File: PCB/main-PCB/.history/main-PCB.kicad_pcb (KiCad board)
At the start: 4 copper layers, 19.9 x 18.2 mm, 25 parts, among them Q1 SSM6J214FE, Q2 Q_NMOS_GSD, U1 LIS2DU12TR, U2 STM32U031K4Ux

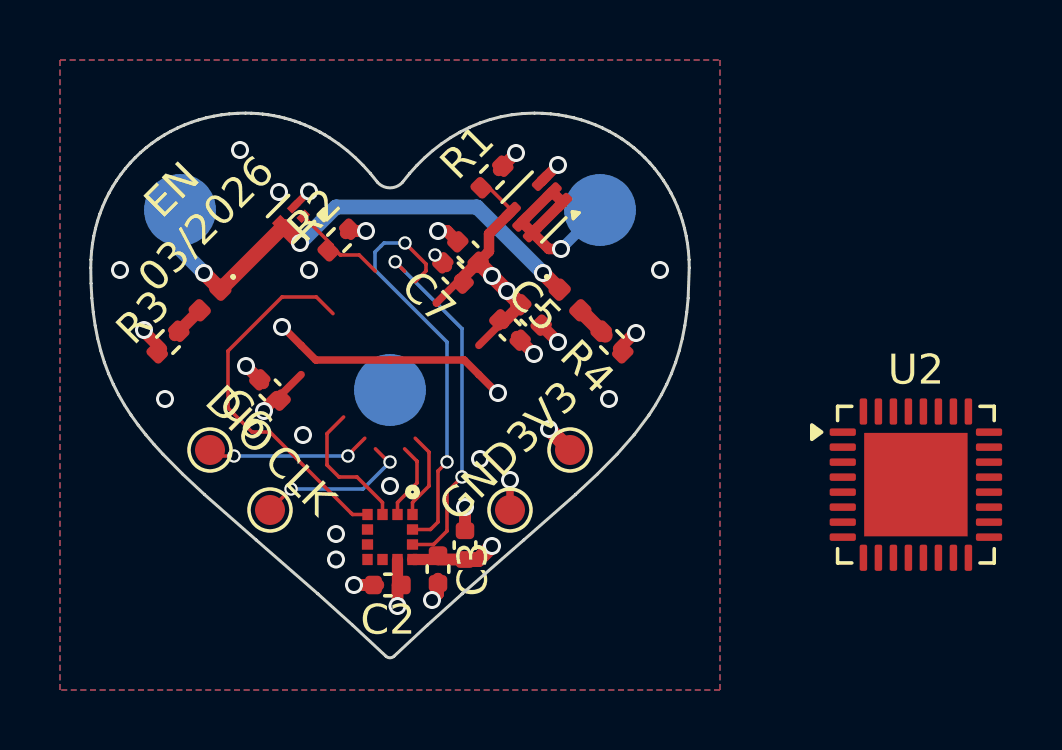
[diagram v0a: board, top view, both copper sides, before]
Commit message: -Updated MCU part number -Changed to 0402 passives
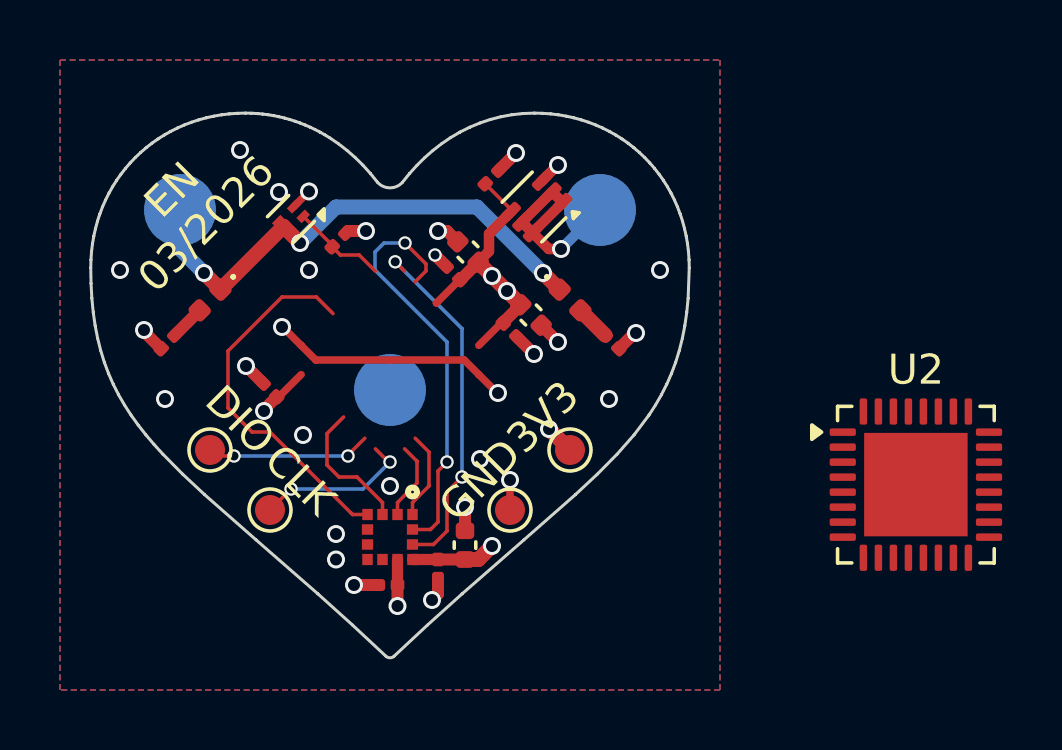
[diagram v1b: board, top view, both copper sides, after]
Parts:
- C2, C3, C5, C6, C7: footprint Capacitor_SMD:C_0402_1005Metric -> Capacitor_SMD:C_0201_0603Metric
- R1, R2, R3, R4: footprint Resistor_SMD:R_0402_1005Metric -> Resistor_SMD:R_0201_0603Metric

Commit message: Updated PCB STEP file
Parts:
- removed the TP5 at (156.0, 93.0)
- added C5: 100nF, Capacitor_SMD:C_0402_1005Metric, F.Cu at (154.7, 91.4)
- added REF**: Val**, EN_Designs-Footprints:JLCPCB_Mouse_Bite, F.Cu at (145.5, 96.3)
- added REF**: Val**, EN_Designs-Footprints:JLCPCB_Mouse_Bite, F.Cu at (156.3, 94.7)
- added REF**: Val**, EN_Designs-Footprints:JLCPCB_Mouse_Bite, F.Cu at (151.1, 99.3)
- added REF**: Val**, EN_Designs-Footprints:JLCPCB_Mouse_Bite, F.Cu at (143.7, 94.7)
- added REF**: Val**, EN_Designs-Footprints:JLCPCB_Mouse_Bite, F.Cu at (151.9, 98.6)
- added REF**: Val**, EN_Designs-Footprints:JLCPCB_Mouse_Bite, F.Cu at (146.4, 97.1)
- added REF**: Val**, EN_Designs-Footprints:JLCPCB_Mouse_Bite, F.Cu at (155.4, 95.5)
- added REF**: Val**, EN_Designs-Footprints:JLCPCB_Mouse_Bite, F.Cu at (142.8, 93.9)
- added REF**: Val**, EN_Designs-Footprints:JLCPCB_Mouse_Bite, F.Cu at (148.9, 99.3)
- added REF**: Val**, EN_Designs-Footprints:JLCPCB_Mouse_Bite, F.Cu at (144.6, 95.5)
- added REF**: Val**, EN_Designs-Footprints:JLCPCB_Mouse_Bite, F.Cu at (147.2, 97.8)
- added REF**: Val**, EN_Designs-Footprints:JLCPCB_Mouse_Bite, F.Cu at (154.5, 96.3)
- added REF**: Val**, EN_Designs-Footprints:JLCPCB_Mouse_Bite, F.Cu at (148.1, 98.6)
- added REF**: Val**, EN_Designs-Footprints:JLCPCB_Mouse_Bite, F.Cu at (153.6, 97.1)
- added REF**: Val**, EN_Designs-Footprints:JLCPCB_Mouse_Bite, F.Cu at (152.8, 97.8)
- added REF**: Val**, EN_Designs-Footprints:JLCPCB_Mouse_Bite, F.Cu at (157.2, 93.9)
- added TP2: TestPoint, TestPoint:TestPoint_Pad_D1.0mm, F.Cu at (157.0, 92.0)
- added TP4: TestPoint, EN_Designs-Footprints:TestPoint_Pad_D0.5mm, F.Cu at (155.7, 90.4)
- C2, C3: footprint Capacitor_SMD:C_0201_0603Metric -> Capacitor_SMD:C_0402_1005Metric
- C6: renamed from C5; footprint Capacitor_SMD:C_0201_0603Metric -> Capacitor_SMD:C_0402_1005Metric
- C7: renamed from C6; footprint Capacitor_SMD:C_0201_0603Metric -> Capacitor_SMD:C_0402_1005Metric
- C8: renamed from C7; footprint Capacitor_SMD:C_0201_0603Metric -> Capacitor_SMD:C_0402_1005Metric
- R1, R2, R3, R4: footprint Resistor_SMD:R_0201_0603Metric -> Resistor_SMD:R_0402_1005Metric
- moved U2 18.0 mm to (150.0, 90.0), turned to -135 degrees
- moved C1 1.50 mm to (153.3, 94.9), turned to 135 degrees
- moved TP5 1.41 mm to (143.0, 92.0)
- moved TP6 1.41 mm to (145.0, 94.0)
- moved TP7 1.41 mm to (155.0, 94.0)
- moved C3 1.26 mm to (152.0, 95.8), turned to 90 degrees
- moved U1 0.40 mm to (150.0, 95.5)
- moved C2 0.26 mm to (149.8, 97.3)
- moved R2 0.23 mm to (148.5, 85.9)
- moved C4 0.19 mm to (154.8, 88.3)
- moved C8 0.19 mm to (152.0, 86.9)
- moved C9 0.19 mm to (152.7, 86.2)
- moved R1 0.18 mm to (153.5, 83.8)
- moved C7 0.17 mm to (145.8, 91.0)
- moved C6 0.14 mm to (154.1, 89.0)
- renumbered C8 to C9, TP2 to TP3, TP3 to TP5, TP4 to TP6, TP6 to TP7, TP7 to TP8
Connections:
- U2 pad 4: unconnected-(U2-PF2-Pad4) -> Net-(U2-PF2)
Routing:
- net Net-(Q1-D-Pad1): track 6.86 -> 14.4 mm
- net Net-(U2-PF2): track 0.00 -> 6.01 mm, vias 0 -> 2
- net GND: track 18.3 -> 22.4 mm, vias 27 -> 29
- net /SWDIO: track 5.51 -> 6.92 mm
- net VCC: track 18.2 -> 19.1 mm, vias 8 -> 7
- net /SWCLK: track 5.33 -> 5.92 mm
- net /MOSI: track 12.5 -> 13.0 mm
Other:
- board size 19.9 x 18.2 mm -> 20 x 18.3 mm
- board text added: "EN 04/2026"
- board text removed: "EN 03/2026"
